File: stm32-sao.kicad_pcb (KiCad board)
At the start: 2 copper layers, 30.5 x 32.4 mm, 41 parts, among them J1 Conn_02x02_Top_Bottom, J2 Conn_02x04_Top_Bottom, J3 Conn_01x04, J4 Conn_01x12_Male, U1 STM32F030F4Px, U2 M24C02-WMN

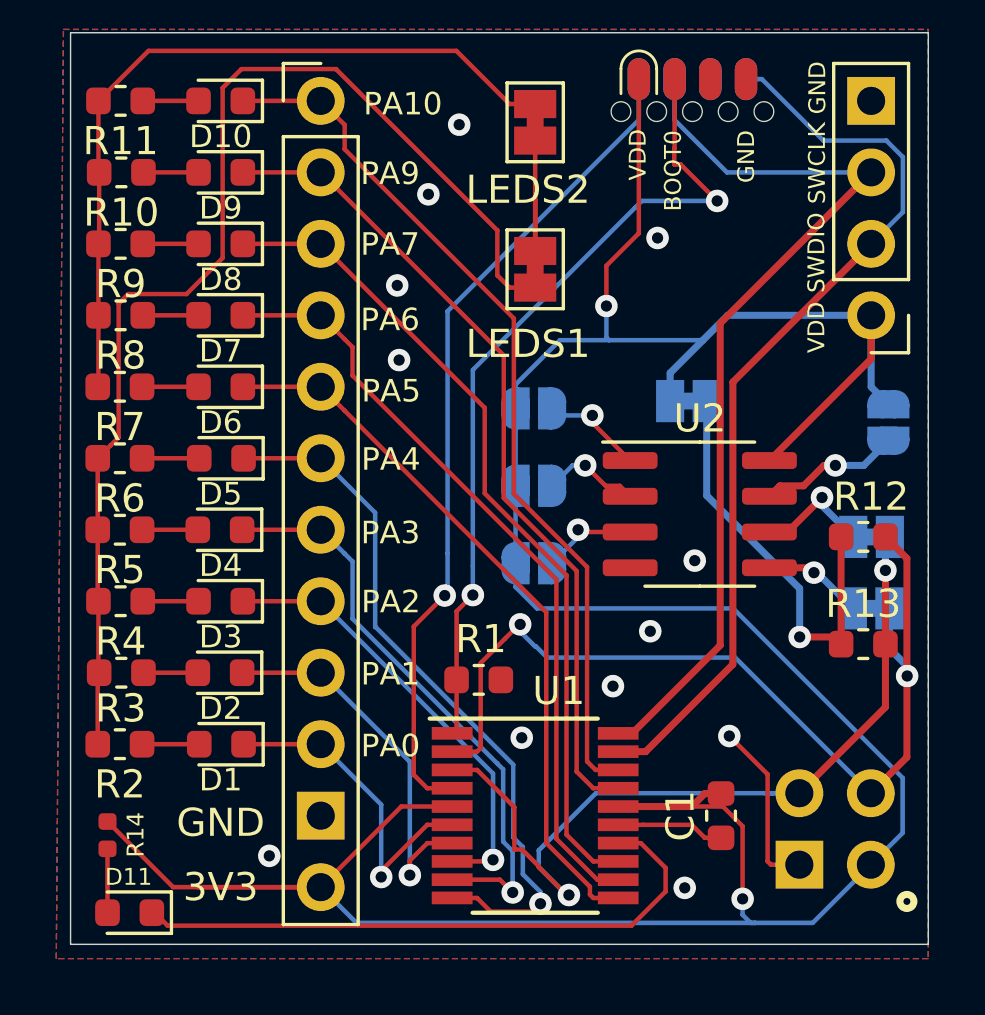
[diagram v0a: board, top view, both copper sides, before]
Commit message: fix: use male connector for SAO
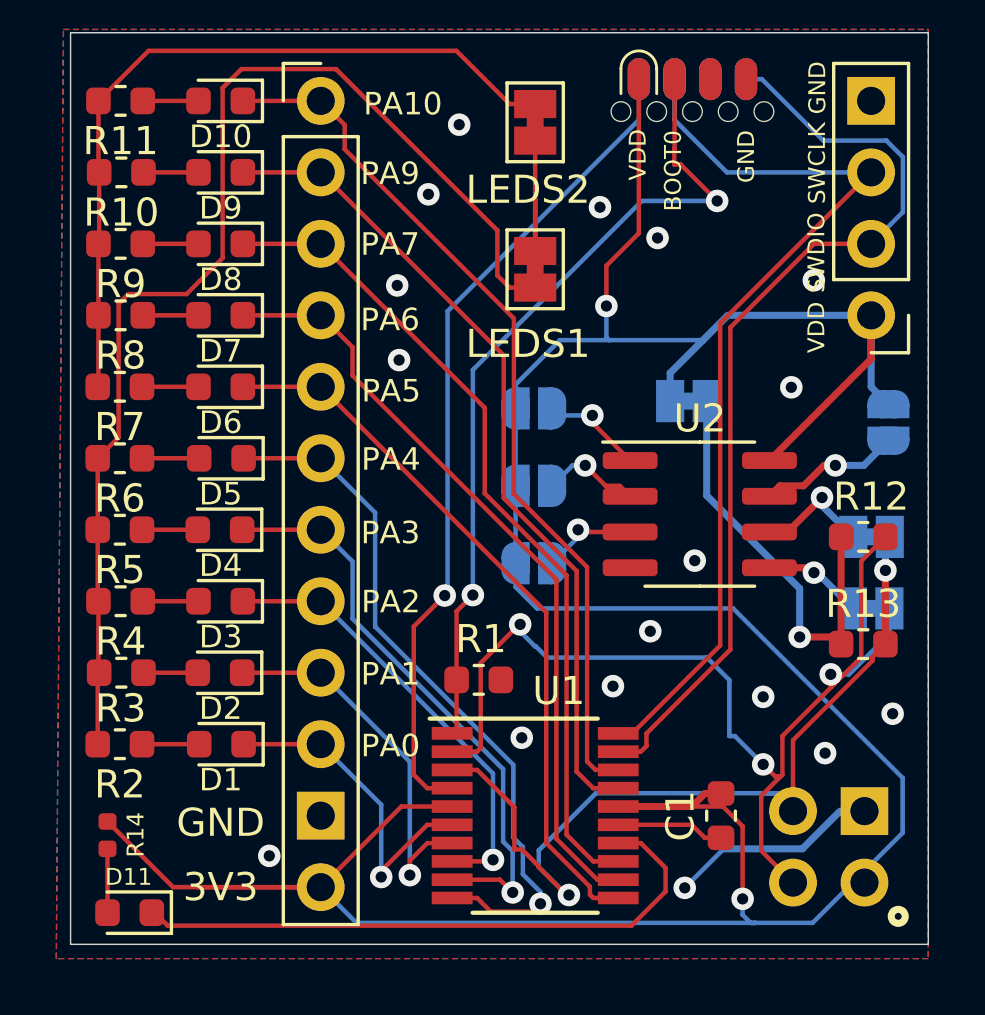
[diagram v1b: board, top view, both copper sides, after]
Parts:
- J1: footprint Connector_PinSocket_2.54mm:PinSocket_2x02_P2.54mm_Vertical -> Connector_PinHeader_2.54mm:PinHeader_2x02_P2.54mm_Vertical
- moved J1 0.67 mm to (135.4, 102.2), turned to 90 degrees
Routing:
- net /SDA: track 33.2 -> 37.3 mm, vias 2 -> 3
- net GND: track 15.8 -> 17.1 mm, vias 12 -> 17
- net /SWDIO: track 32.6 -> 33.7 mm
- net /SCL: track 29.6 -> 30.4 mm

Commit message: fix: optimize tracks + silk screen for pin 1
reduce track width, remove unused tracks,
mark UC pin 1 with a circle on silk screen
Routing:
- net VDD: track 113.5 -> 112.1 mm

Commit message: fix: LEDs connected wrong
they should be connected to VCC, not GND!
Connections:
- JP7 pad 2: GND -> VDD
- JP8 pad 2: GND -> VDD
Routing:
- net VDD: track 112.1 -> 122.4 mm
- net GND: track 17.1 -> 11.4 mm, vias 17 -> 18
- net Net-(JP7-Pad1): track 42.0 -> 43.5 mm
- net Net-(D1-Pad1): track 11.8 -> 13.3 mm
- net Net-(D8-Pad1): track 29.6 -> 31.0 mm
- net Net-(D6-Pad1): track 25.8 -> 26.4 mm

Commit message: fix: wrong I2C pins
PA9/PA10 should be connected to the I2C bus instead of PF0/PF1
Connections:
- D10 pad 1: Net-(D10-Pad1) -> /LED10
- D9 pad 1: Net-(D9-Pad1) -> /LED9
- J4 pad 1: Net-(D10-Pad1) -> /LED10
- J4 pad 2: Net-(D9-Pad1) -> /LED9
- U1 pad 17: Net-(D9-Pad1) -> /SCL
- U1 pad 18: Net-(D10-Pad1) -> /SDA
- U1 pad 2: /SDA -> /LED9
- U1 pad 3: /SCL -> /LED10
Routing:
- net Net-(D10-Pad1): track 31.4 -> 0.00 mm
- net /LED10: track 0.00 -> 30.2 mm, vias 0 -> 1
- net Net-(D9-Pad1): track 29.6 -> 0.00 mm
- net /LED9: track 0.00 -> 26.4 mm, vias 0 -> 1
- net /SDA: track 37.3 -> 29.9 mm, vias 3 -> 2
- net /SCL: track 30.4 -> 32.0 mm
- net VDD: track 122.4 -> 123.1 mm
- net GND: track 11.4 -> 12.0 mm, vias 18 -> 19

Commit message: fix: silk screen
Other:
- board text added: "PF0"
- board text added: "PF1"
- board text removed: "PA10"
- board text removed: "PA9"
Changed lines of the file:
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@@
   )
   (setup
-    (last_trace_width 0.16)
+    (last_trace_width 0.25)
     (user_trace_width 0.16)
     (trace_clearance 0.2)
@@
     (effects (font (size 0.6 0.6) (thickness 0.1)))
   )
-  (gr_text PA10 (at 118.99646 74.53122) (layer F.SilkS)
+  (gr_text PF1 (at 118.54434 74.53122) (layer F.SilkS)
     (effects (font (size 0.8 0.8) (thickness 0.1)))
   )
-  (gr_text PA9 (at 118.54434 77.00518) (layer F.SilkS)
+  (gr_text PF0 (at 118.54434 77.00518) (layer F.SilkS)
     (effects (font (size 0.8 0.8) (thickness 0.1)))
   )

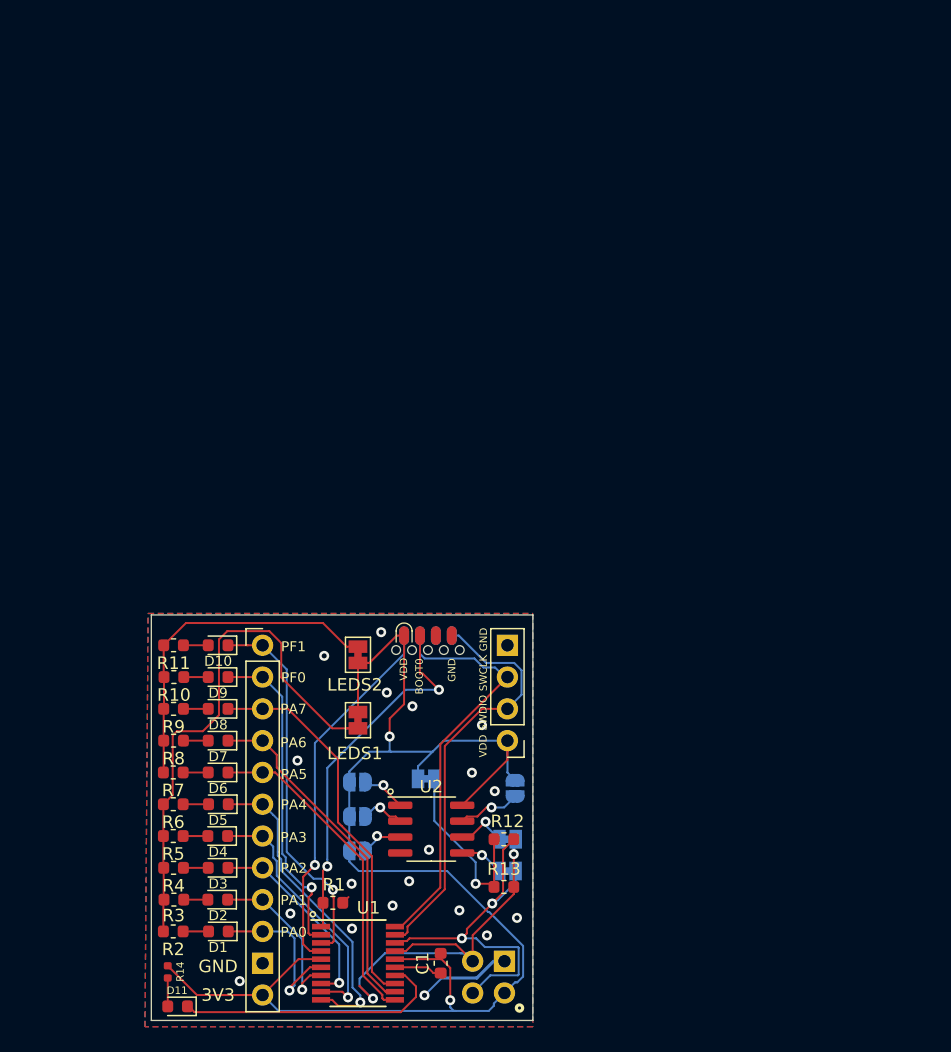
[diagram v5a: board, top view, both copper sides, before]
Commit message: feat: second version of the PCB
1. Upgrade #badgelife Shitty Add-On connector to V1.69bis
2. Add 10 NeoPixels (WS2812B-Mini)
3. Add a small 7mm speaker
4. Redesign the board
5. Add a second I2C EEPROM
6. Add AramCon conference logo
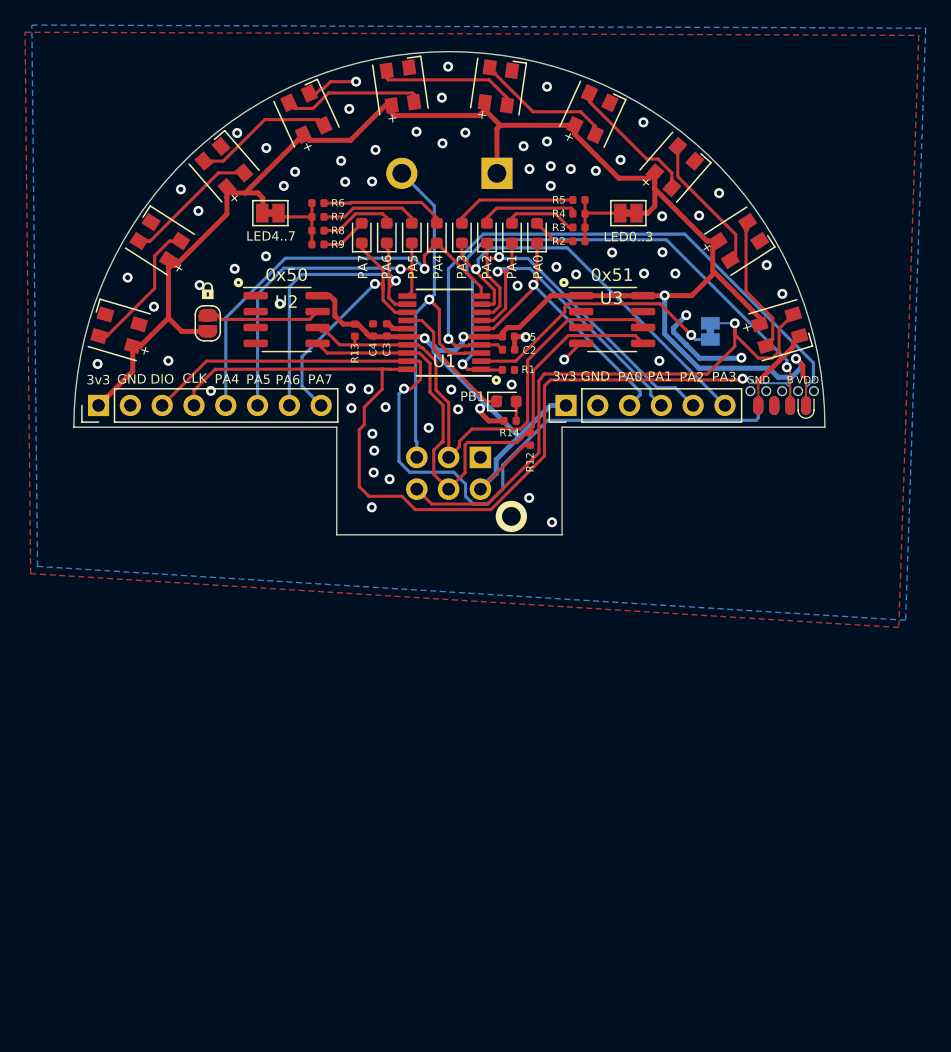
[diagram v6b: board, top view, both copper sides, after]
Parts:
- removed C1: 1uF, Capacitor_SMD:C_0603_1608Metric
- removed D10, D9: LED, LED_SMD:LED_0603_1608Metric
- removed J3: Conn_01x04, Connector_PinHeader_2.54mm:PinHeader_1x04_P2.54mm_Vertical
- removed JP2: E1, Jumper:SolderJumper-2_P1.3mm_Open_RoundedPad1.0x1.5mm
- removed JP3: E2, Jumper:SolderJumper-2_P1.3mm_Open_RoundedPad1.0x1.5mm
- removed JP5: SDA, Jumper:SolderJumper-2_P1.3mm_Bridged_Pad1.0x1.5mm
- removed JP6: SCL, Jumper:SolderJumper-2_P1.3mm_Bridged_Pad1.0x1.5mm
- removed JP9: I2C_PULLUP, Jumper:SolderJumper-2_P1.3mm_Bridged_Pad1.0x1.5mm
- removed R10, R11: 4.7k, Resistor_SMD:R_0603_1608Metric
- added C2: 1uF, Capacitor_SMD:C_0402_1005Metric, F.Cu at (135.7, 50.8)
- added C3: 100nF, Capacitor_SMD:C_0402_1005Metric, F.Cu at (126.0, 49.2)
- added C4: 4.7uF, Capacitor_SMD:C_0402_1005Metric, F.Cu at (124.9, 49.2)
- added C5: 1uF, Capacitor_SMD:C_0402_1005Metric, F.Cu at (135.7, 49.8)
- added D12: WS2812B, AramCon:LED-SMD_4P-L3.5-W3.5-TL_WS2812B, F.Cu at (157.4, 49.3)
- added D13: WS2812B, AramCon:LED-SMD_4P-L3.5-W3.5-TL_WS2812B, F.Cu at (154.1, 42.1)
- added D14: WS2812B, AramCon:LED-SMD_4P-L3.5-W3.5-TL_WS2812B, F.Cu at (149.0, 36.2)
- added D15: WS2812B, AramCon:LED-SMD_4P-L3.5-W3.5-TL_WS2812B, F.Cu at (142.4, 32.0)
- added D16: WS2812B, AramCon:LED-SMD_4P-L3.5-W3.5-TL_WS2812B, F.Cu at (134.9, 29.8)
- added D17: WS2812B, AramCon:LED-SMD_4P-L3.5-W3.5-TL_WS2812B, F.Cu at (127.1, 29.8)
- added D18: WS2812B, AramCon:LED-SMD_4P-L3.5-W3.5-TL_WS2812B, F.Cu at (119.6, 32.0)
- added D19: WS2812B, AramCon:LED-SMD_4P-L3.5-W3.5-TL_WS2812B, F.Cu at (113.0, 36.2)
- added D20: WS2812B, AramCon:LED-SMD_4P-L3.5-W3.5-TL_WS2812B, F.Cu at (107.9, 42.1)
- added D21: WS2812B, AramCon:LED-SMD_4P-L3.5-W3.5-TL_WS2812B, F.Cu at (104.6, 49.3)
- added LS1: Speaker, AramCon:BUZZER-R14-2P-7.6PITCH, B.Cu at (131.0, 36.7)
- added U3: AT24C256C, Package_SO:SOIC-8_3.9x4.9mm_P1.27mm, F.Cu at (144.0, 48.4)
- added X1: Badgelife_sao_connector_v169bis, AramCon:Badgelife-SAOv169-SAO-2x3, F.Cu at (131.0, 60.7)
- added svg2mod: G***, AramCon:aramcon-logo-2, B.Cu at (130.8, 47.8)
- added svg2mod: G***, AramCon:lock, F.Cu at (111.7, 46.1)
- J1: value Conn_02x02_Top_Bottom -> Conn_01x06_Male; footprint Connector_PinHeader_2.54mm:PinHeader_2x02_P2.54mm_Vertical -> Connector_PinHeader_2.54mm:PinHeader_1x06_P2.54mm_Vertical; moved to F.Cu
- J4: value Conn_01x12_Male -> Conn_01x08_Male; footprint Connector_PinHeader_2.54mm:PinHeader_1x12_P2.54mm_Vertical -> Connector_PinHeader_2.54mm:PinHeader_1x08_P2.54mm_Vertical
- JP1: value E0 -> SolderJumper_2_Bridged; footprint Jumper:SolderJumper-2_P1.3mm_Open_RoundedPad1.0x1.5mm -> Jumper:SolderJumper-2_P1.3mm_Bridged_Pad1.0x1.5mm
- JP4: moved to F.Cu
- R1, R12, R13, R2, R3, R4, R5, R6, R7, R8, R9: footprint Resistor_SMD:R_0603_1608Metric -> Resistor_SMD:R_0402_1005Metric
- moved R2 64.0 mm to (141.3, 42.1), turned to 0 degrees
- moved R3 62.7 mm to (141.3, 41.0), turned to 0 degrees
- moved R4 61.5 mm to (141.3, 40.0), turned to 0 degrees
- moved D1 61.3 mm to (138.0, 41.5), turned to 90 degrees
- moved R5 60.3 mm to (141.3, 38.9), turned to 0 degrees
- moved D2 58.2 mm to (136.0, 41.5), turned to 90 degrees
- moved D3 55.1 mm to (134.0, 41.5), turned to 90 degrees
- moved D11 55.0 mm to (135.6, 55.0), turned to 0 degrees
- moved D4 52.0 mm to (132.0, 41.5), turned to 90 degrees
- moved R14 51.8 mm to (135.8, 56.5), turned to 0 degrees
- moved U1 50.8 mm to (130.6, 49.5), turned to 180 degrees
- moved R6 49.4 mm to (120.5, 39.1)
- moved D5 48.8 mm to (130.0, 41.5), turned to 90 degrees
- moved J1 47.2 mm to (140.3, 55.3)
- moved R13 46.0 mm to (123.5, 49.2), turned to 270 degrees
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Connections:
- D1 pad 1: Net-(D1-Pad1) -> /GPIO0
- D2 pad 1: Net-(D2-Pad1) -> /GPIO1
- D3 pad 1: Net-(D3-Pad1) -> /GPIO2
- D4 pad 1: Net-(D4-Pad1) -> /GPIO3
- D5 pad 1: Net-(D5-Pad1) -> /GPIO4
- D6 pad 1: Net-(D6-Pad1) -> /GPIO5
- D7 pad 1: Net-(D7-Pad1) -> /GPIO6
- D8 pad 1: Net-(D8-Pad1) -> /GPIO7
- J1 pad 3: /SDA -> /GPIO0
- J1 pad 4: /SCL -> /GPIO1
- J4 pad 1: /LED10 -> VDD
- J4 pad 2: /LED9 -> GND
- J4 pad 3: Net-(D8-Pad1) -> /SWDIO
- J4 pad 4: Net-(D7-Pad1) -> /SWCLK
- J4 pad 5: Net-(D6-Pad1) -> /GPIO4
- J4 pad 6: Net-(D5-Pad1) -> /GPIO5
- J4 pad 7: Net-(D4-Pad1) -> /GPIO6
- J4 pad 8: Net-(D3-Pad1) -> /GPIO7
- JP1 pad 1: VDD -> /NEOPIXELS
- R12 pad 1: Net-(JP9-Pad2) -> VDD
- R13 pad 1: Net-(JP9-Pad2) -> VDD
- R6 pad 2: Net-(JP7-Pad1) -> Net-(JP8-Pad1)
- U1 pad 10: Net-(D5-Pad1) -> /GPIO4
- U1 pad 11: Net-(D6-Pad1) -> /GPIO5
- U1 pad 12: Net-(D7-Pad1) -> /GPIO6
- U1 pad 13: Net-(D8-Pad1) -> /GPIO7
- U1 pad 2: /LED9 -> Net-(JP1-Pad2)
- U1 pad 3: /LED10 -> /SPEAKER
- U1 pad 6: Net-(D1-Pad1) -> /GPIO0
- U1 pad 7: Net-(D2-Pad1) -> /GPIO1
- U1 pad 8: Net-(D3-Pad1) -> /GPIO2
- U1 pad 9: Net-(D4-Pad1) -> /GPIO3
- U2 pad 1: Net-(JP1-Pad2) -> Net-(U2-Pad1)
- U2 pad 5: Net-(JP5-Pad1) -> /SDA
- U2 pad 6: Net-(JP6-Pad1) -> /SCL
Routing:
- net VDD: track 123.1 -> 182.6 mm, vias 2 -> 5
- net /NEOPIXELS: track 0.00 -> 47.2 mm, vias 0 -> 1
- net /SWCLK: track 33.2 -> 74.1 mm, vias 0 -> 1
- net Net-(JP7-Pad1): track 43.5 -> 6.14 mm
- net /GPIO3: track 0.00 -> 33.5 mm, vias 0 -> 1
- net /GPIO4: track 0.00 -> 33.4 mm, vias 0 -> 1
- net /SWDIO: track 33.7 -> 67.0 mm, vias 0 -> 1
- net /SPEAKER: track 0.00 -> 31.9 mm, vias 0 -> 1
- net Net-(D8-Pad1): track 31.0 -> 0.00 mm
- net /LED10: track 30.2 -> 0.00 mm, vias 1 -> 0
- net /GPIO2: track 0.00 -> 28.7 mm, vias 0 -> 1
- net Net-(D7-Pad1): track 27.6 -> 0.00 mm
- net /GPIO5: track 0.00 -> 26.7 mm, vias 0 -> 1
- net Net-(D6-Pad1): track 26.4 -> 0.00 mm
- net /GPIO1: track 0.00 -> 26.4 mm, vias 0 -> 1
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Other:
- board size 30.5 x 32.4 mm -> 60 x 38.6 mm
- board text added: "0x50"
- board text added: "0x51"
- board text added: "3v3"
- board text added: "B"
- board text added: "CLK"
- board text added: "DIO"
- board text added: "LED0..3"
- board text added: "LED4..7"
- board text added: "NeoPixels"
- board text added: "PB1"
- board text added: "STM32"
- board text added: "© 2020, Uri Shaked"
- board text removed: "3V3"
- board text removed: "BOOT0"
- board text removed: "PF0"
- board text removed: "PF1"
- board text removed: "© 2019, Uri Shaked"

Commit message: feat: add background pattern to back side
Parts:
- added Ref**: Val**, AramCon:background, B.Cu at (131.2, 42.6)
